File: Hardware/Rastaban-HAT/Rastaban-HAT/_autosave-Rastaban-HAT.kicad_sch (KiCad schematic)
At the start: 75 parts, among them IC1 BCR420UW6-7, J1 1778780, J10 GPIO, J11 Conn_01x06_Male, J12 Conn_01x03_Male, J2 1778780, J3 1778780, J4 Screw_Terminal_01x02, J5 Jack-DC 12V+, J6 SM04B-SRSS-TB(LF)(SN)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

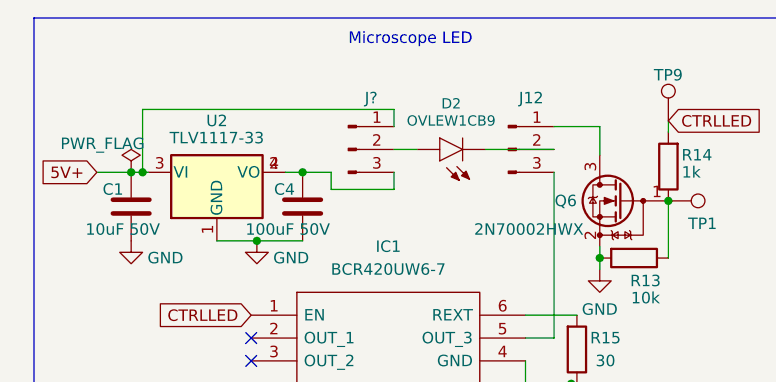
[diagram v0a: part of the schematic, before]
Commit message: started routing biger traces
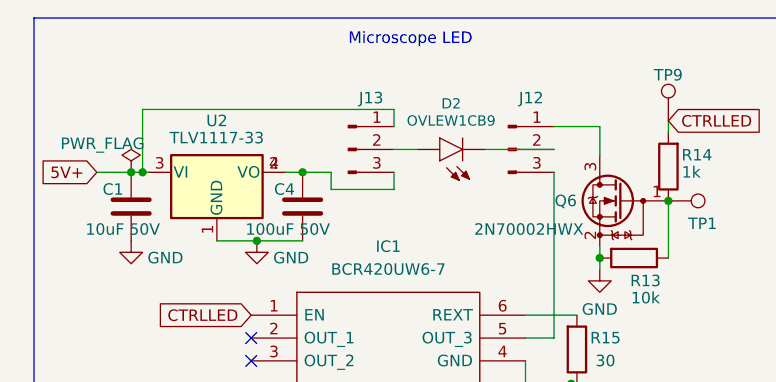
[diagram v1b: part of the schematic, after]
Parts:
- gave numbers to parts that had none: 1
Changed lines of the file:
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@@
   (symbol (lib_id "Connector:Conn_01x03_Male") (at 47.625 27.305 0) (unit 1)
     (in_bom yes) (on_board yes)
-    (property "Reference" "J?" (id 0) (at 50.165 21.59 0))
+    (property "Reference" "J13" (id 0) (at 50.165 21.59 0))
     (property "Value" "Conn_01x03_Male" (id 1) (at 48.26 21.59 0)
       (effects (font (size 1.27 1.27)) hide)
@@
     )
     (path "/1ea964af-da3d-44fa-847d-b6df7f6e3ab6"
-      (reference "J?") (unit 1) (value "Conn_01x03_Male") (footprint "Connector_PinSocket_2.54mm:PinSocket_1x03_P2.54mm_Vertical")
+      (reference "J13") (unit 1) (value "Conn_01x03_Male") (footprint "Connector_PinSocket_2.54mm:PinSocket_1x03_P2.54mm_Vertical")
     )
     (path "/d76e85fc-4f2e-4d54-b404-7aa3a9abd669"
